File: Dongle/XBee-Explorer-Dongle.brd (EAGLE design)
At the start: 40.6 x 27.9 mm, 38 parts, among them U2 XBEE-1B3, U3 MIC5205 3.3V, U4 FT231XS

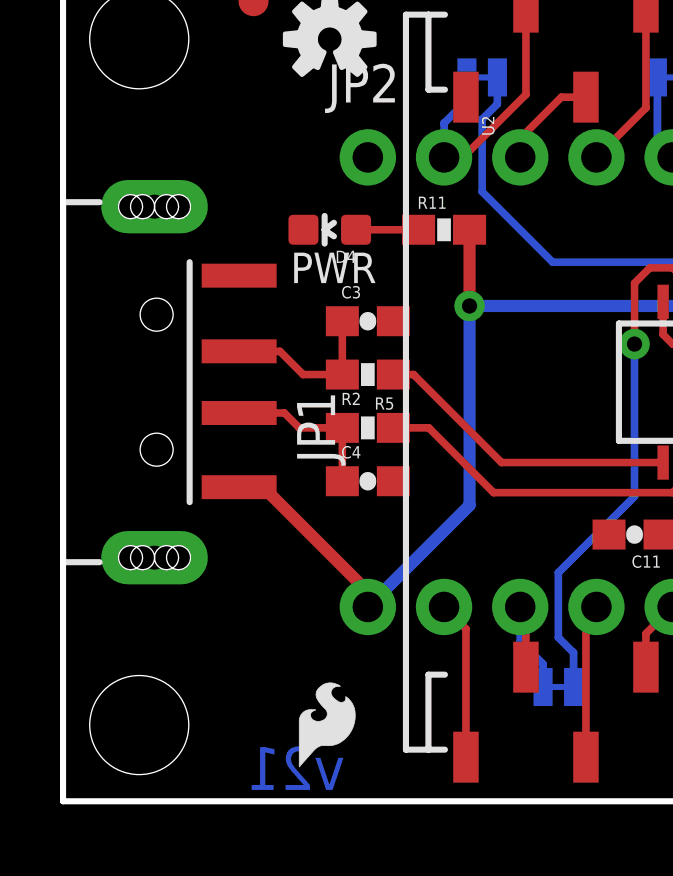
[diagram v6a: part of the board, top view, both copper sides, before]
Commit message: Updating USB dongle connector to use locking fp
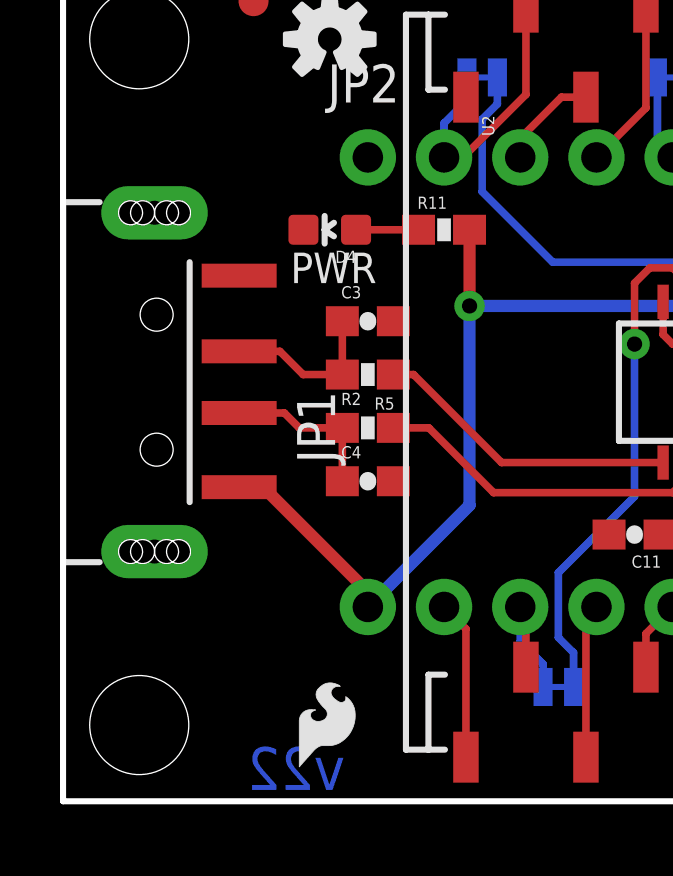
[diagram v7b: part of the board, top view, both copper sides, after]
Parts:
- JP1: value USBA-SMD-MALE -> USBA-SMD-MALE-LOCKING; device SparkFun-Connectors:USB-A-SMT-MALE -> SparkFun-Connectors:USB-A-SMT-MALE-LOCKING
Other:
- board text added: "v22"
- board text removed: "v21"
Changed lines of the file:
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@@
 <layer number="54" name="bGND_GNDA" color="1" fill="9" visible="no" active="no"/>
 <layer number="56" name="wert" color="7" fill="1" visible="no" active="yes"/>
+<layer number="57" name="tCAD" color="7" fill="1" visible="no" active="no"/>
 <layer number="91" name="Nets" color="2" fill="1" visible="no" active="no"/>
 <layer number="92" name="Busses" color="1" fill="1" visible="no" active="no"/>
@@
 <layer number="97" name="Info" color="7" fill="1" visible="no" active="no"/>
 <layer number="98" name="Guide" color="6" fill="1" visible="no" active="no"/>
+<layer number="99" name="SpiceOrder" color="7" fill="1" visible="no" active="no"/>
 <layer number="100" name="Muster" color="7" fill="1" visible="no" active="no"/>
 <layer number="101" name="Patch_Top" color="12" fill="4" visible="no" active="yes"/>
@@
 <layer number="108" name="tplace-old" color="10" fill="1" visible="no" active="yes"/>
 <layer number="109" name="ref-old" color="11" fill="1" visible="no" active="yes"/>
-<layer number="110" name="fp0" color="7" fill="1" visible="yes" active="yes"/>
-<layer number="111" name="LPC17xx" color="7" fill="1" visible="yes" active="yes"/>
-<layer number="112" name="tSilk" color="7" fill="1" visible="yes" active="yes"/>
-<layer number="113" name="IDFDebug" color="4" fill="1" visible="yes" active="yes"/>
+<layer number="110" name="fp0" color="7" fill="1" visible="no" active="yes"/>
+<layer number="111" name="LPC17xx" color="7" fill="1" visible="no" active="yes"/>
+<layer number="112" name="tSilk" color="7" fill="1" visible="no" active="yes"/>
+<layer number="113" name="IDFDebug" color="4" fill="1" visible="no" active="yes"/>
 <layer number="116" name="Patch_BOT" color="9" fill="4" visible="no" active="yes"/>
 <layer number="121" name="_tsilk" color="7" fill="1" visible="no" active="yes"/>
 <layer number="122" name="_bsilk" color="7" fill="1" visible="no" active="yes"/>
-<layer number="123" name="tTestmark" color="7" fill="1" visible="yes" active="yes"/>
-<layer number="124" name="bTestmark" color="7" fill="1" visible="yes" active="yes"/>
+<layer number="123" name="tTestmark" color="7" fill="1" visible="no" active="yes"/>
+<layer number="124" name="bTestmark" color="7" fill="1" visible="no" active="yes"/>
 <layer number="125" name="_tNames" color="7" fill="1" visible="no" active="yes"/>
-<layer number="126" name="_bNames" color="7" fill="1" visible="yes" active="yes"/>
-<layer number="127" name="_tValues" color="7" fill="1" visible="yes" active="yes"/>
-<layer number="128" name="_bValues" color="7" fill="1" visible="yes" active="yes"/>
-<layer number="131" name="tAdjust" color="7" fill="1" visible="yes" active="yes"/>
-<layer number="132" name="bAdjust" color="7" fill="1" visible="yes" active="yes"/>
+<layer number="126" name="_bNames" color="7" fill="1" visible="no" active="yes"/>
+<layer number="127" name="_tValues" color="7" fill="1" visible="no" active="yes"/>
+<layer number="128" name="_bValues" color="7" fill="1" visible="no" active="yes"/>
+<layer number="131" name="tAdjust" color="7" fill="1" visible="no" active="yes"/>
+<layer number="132" name="bAdjust" color="7" fill="1" visible="no" active="yes"/>
 <layer number="144" name="Drill_legend" color="7" fill="1" visible="no" active="yes"/>
+<layer number="150" name="Notes" color="7" fill="1" visible="yes" active="yes"/>
 <layer number="151" name="HeatSink" color="7" fill="1" visible="no" active="yes"/>
-<layer number="152" name="_bDocu" color="7" fill="1" visible="yes" active="yes"/>
+<layer number="152" name="_bDocu" color="7" fill="1" visible="no" active="yes"/>
+<layer number="153" name="FabDoc1" color="7" fill="1" visible="yes" active="yes"/>
+<layer number="154" name="FabDoc2" color="7" fill="1" visible="yes" active="yes"/>
+<layer number="155" name="FabDoc3" color="7" fill="1" visible="yes" active="yes"/>
 <layer number="199" name="Contour" color="7" fill="1" visible="no" active="yes"/>
 <layer number="200" name="200bmp" color="1" fill="10" visible="no" active="no"/>
@@
 <layer number="223" name="223bmp" color="24" fill="1" visible="no" active="no"/>
 <layer number="224" name="224bmp" color="25" fill="1" visible="no" active="no"/>
-<layer number="248" name="Housing" color="7" fill="1" visible="yes" active="yes"/>
-<layer number="249" name="Edge" color="7" fill="1" visible="yes" active="yes"/>
+<layer number="248" name="Housing" color="7" fill="1" visible="no" active="yes"/>
+<layer number="249" name="Edge" color="7" fill="1" visible="no" active="yes"/>
 <layer number="250" name="Descript" color="3" fill="1" visible="no" active="no"/>
 <layer number="251" name="SMDround" color="12" fill="11" visible="no" active="no"/>
@@
 <text x="9.652" y="7.874" size="1.016" layer="22" ratio="15" rot="MR90">5V</text>
 <text x="36.068" y="20.066" size="1.016" layer="22" ratio="15" rot="MR270">GND</text>
-<text x="9.398" y="0.381" size="1.4224" layer="16" font="vector" ratio="20" rot="MR0">v21</text>
+<text x="9.398" y="0.381" size="1.4224" layer="16" font="vector" ratio="20" rot="MR0">v22</text>
 <text x="20.32" y="25.781" size="0.889" layer="22" font="vector" ratio="15" rot="MR0" align="center">RSSI</text>
 <wire x1="19.812" y1="24.13" x2="20.828" y2="24.13" width="0.4064" layer="30"/>
@@
 <element name="JP2" library="SparkFun" package="1X11_NO_SILK" value="M111X11_NO_SILK" x="10.16" y="21.463"/>
 <element name="U$8" library="SparkFun" package="OSHW-LOGO-S" value="OSHW-LOGOS" x="10.16" y="13.97" rot="MR0"/>
-<element name="JP1" library="SparkFun-Connectors" package="USB-A-SMT-MALE" value="USBA-SMD-MALE" x="0" y="13.97" rot="R90"/>
+<element name="JP1" library="SparkFun-Connectors" package="USB-A-SMT-MALE-LOCKING" value="USBA-SMD-MALE-LOCKING" x="0" y="13.97" rot="R90"/>
 <element name="U4" library="SparkFun-DigitalIC" package="SSOP20_L" value="FT231XS" x="22.86" y="13.97" rot="R180"/>
 <element name="R2" library="SparkFun" package="0603-RES" value="27" x="10.16" y="12.446"/>

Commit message: Updating VREG part information
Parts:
- U3: value MIC5205 3.3V -> MIC5219 3.3V
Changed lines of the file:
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@@
 <attribute name="VALUE" x="20.574" y="18.923" size="0.4064" layer="27"/>
 </element>
-<element name="U3" library="SparkFun" package="SOT23-5" value="MIC5205 3.3V" x="31.75" y="16.51" rot="R270"/>
+<element name="U3" library="SparkFun" package="SOT23-5" value="MIC5219 3.3V" x="31.75" y="16.51" rot="R270"/>
 <element name="C1" library="SparkFun" package="EIA3216" value="10uF" x="31.75" y="12.7"/>
 <element name="C2" library="SparkFun" package="0603-CAP" value="0.1uF" x="31.75" y="19.05" rot="R180"/>
